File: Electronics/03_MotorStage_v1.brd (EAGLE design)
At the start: 100 x 80 mm, 77 parts, among them J1 BARRIER_BLOCK-2PIN, J2 BARRIER_BLOCK-5PIN, J3 CONN_2X3_SMD, U1 XL4016-DEV

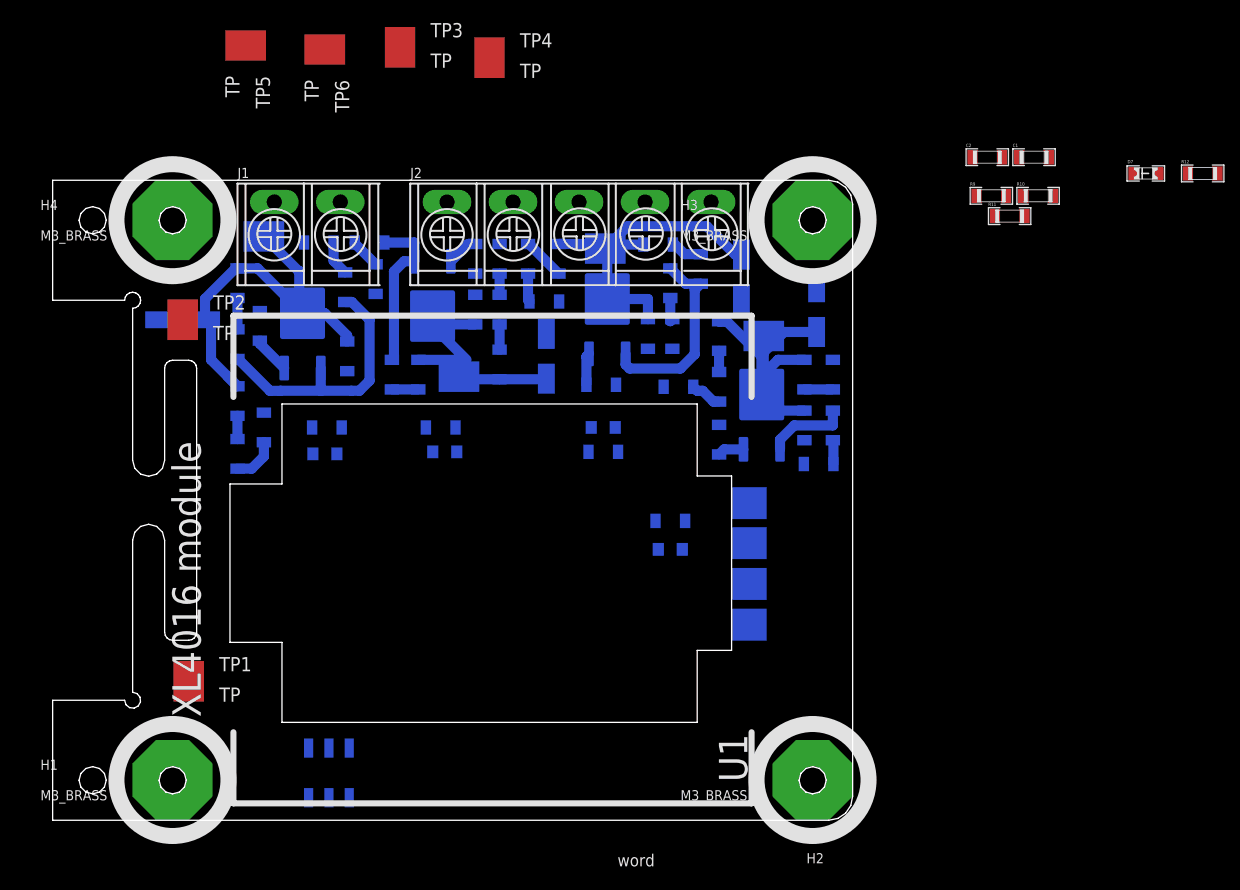
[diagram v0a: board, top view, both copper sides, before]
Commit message: Completed routing of components on motor stage power supply board
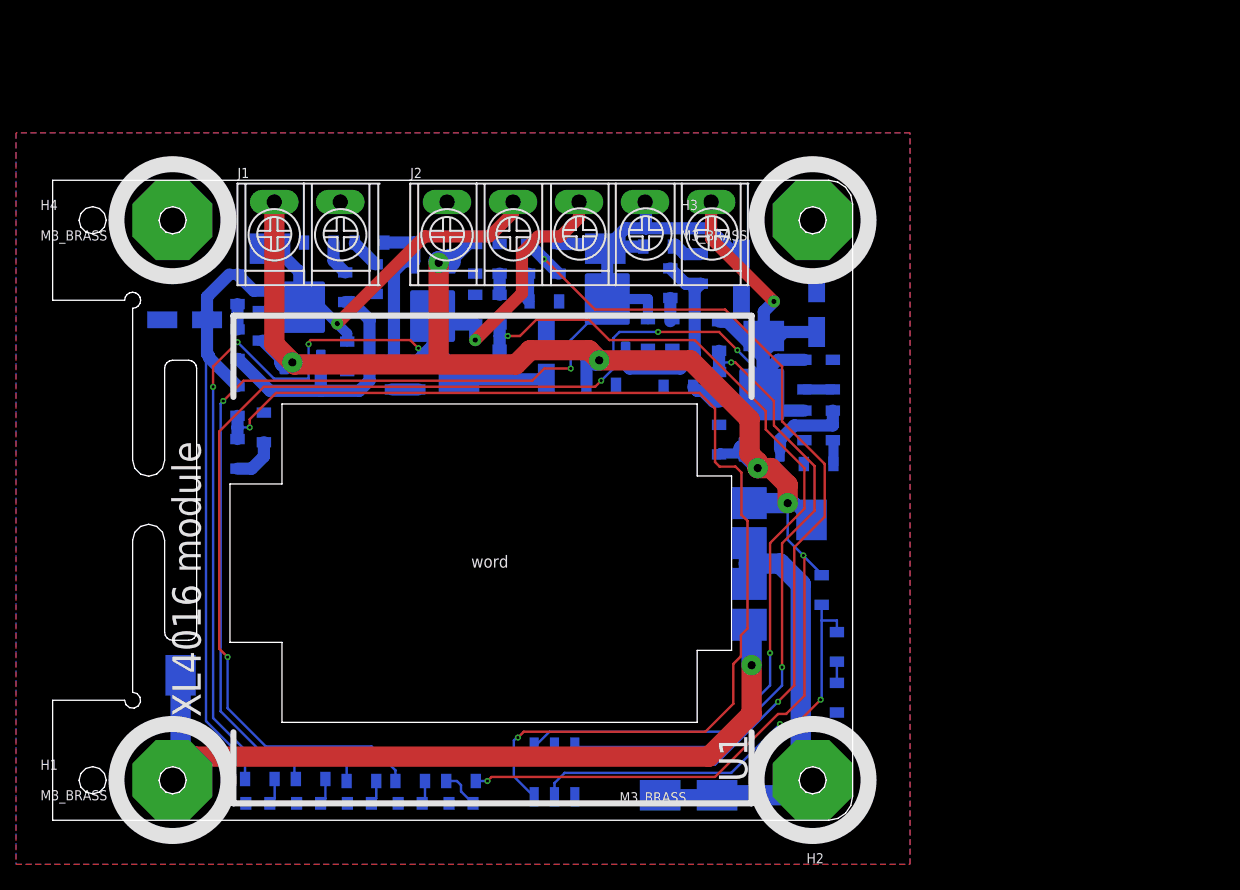
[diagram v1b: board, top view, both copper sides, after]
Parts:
- removed C1: 0.33 uF, standardparts:1206
- removed C2: 10 uF, standardparts:1206
- removed TP5, TP6: TP, Hippo-PS:TP
- C10, C4, C6, C8: value (none) -> 22 uF
- C3, C5, C7, C9: value (none) -> 10 uF
- D7: value YELLOW -> ORANGE
- R10: value 2K -> 4.7K
- R11: value 220 -> 330
- R12: value 220 -> 470
- moved R12 119.8 mm to (68.3, 23.1), flipped to the bottom
- moved D7 116.3 mm to (68.3, 20.3), flipped to the bottom
- moved TP4 94.6 mm to (93.2, 21.3), flipped to the bottom, turned to 270 degrees
- moved TP2 89.4 mm to (100.3, 21.3), flipped to the bottom, turned to 90 degrees
- moved TP3 78.3 mm to (112.1, 55.8), flipped to the bottom
- moved R11 64.0 mm to (115.3, 33.5), flipped to the bottom, turned to 270 degrees
- moved R10 61.7 mm to (115.3, 39.9), flipped to the bottom, turned to 270 degrees
- moved D3 56.0 mm to (55.6, 20.3)
- moved R9 53.6 mm to (113.4, 47.0), flipped to the bottom, turned to 270 degrees
- moved R31 51.1 mm to (55.9, 23.1), turned to 180 degrees
- moved D2 47.1 mm to (49.3, 20.3)
- moved R22 46.9 mm to (49.5, 23.4), turned to 180 degrees
- moved R40 46.0 mm to (62.0, 23.1), turned to 180 degrees
- moved D4 45.4 mm to (62.0, 20.3)
- moved R13 44.7 mm to (43.2, 23.4)
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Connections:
- removed net N$2: U1.IN-, U1.OUT-
- new net IN+: H1.P$1, H3.P$1, TP1.P$1, U1.IN+
- new net N$1: D7.P$1, R12.2
- new net N$23: R10.2, R11.1
- new net SIG_SMPS: J3.4, R10.1, R9.2
- net GND: now also D7.P$2, H2.P$1, H4.P$1, J2.P$1, J3.6, R11.2, TP2.P$1, TP4.P$1, U1.IN-, U1.OUT-
- net OUT1: now also J2.P$2
- net OUT2: now also J2.P$3
- net OUT3: now also J2.P$4
- net OUT4: now also J2.P$5
- net SIG1: now also J3.2
- net SIG2: now also J3.1
- net SIG3: now also J3.3
- net SIG4: now also J3.5
- net V+: now also R12.1, R9.1, TP3.P$1, U1.OUT+
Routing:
- net V+: track 15.9 -> 213.8 mm, vias 0 -> 7
- net OUT4: track 47.0 -> 208.0 mm, vias 0 -> 5
- net SIG1: track 2.90 -> 143.7 mm, vias 0 -> 2
- net OUT3: track 44.7 -> 163.2 mm, vias 0 -> 2
- net OUT2: track 31.4 -> 148.8 mm, vias 0 -> 5
- net SIG3: track 5.34 -> 120.2 mm, vias 0 -> 2
- net SIG2: track 3.16 -> 112.7 mm, vias 0 -> 2
- net IN+: track 0.00 -> 100.6 mm, vias 0 -> 1
- net OUT1: track 50.1 -> 130.7 mm, vias 0 -> 1
- net SIG4: track 2.65 -> 79.9 mm, vias 0 -> 2
- net GND: track 0.00 -> 57.7 mm
- net SIG_SMPS: track 0.00 -> 54.6 mm, vias 0 -> 2
- net N$1: track 0.00 -> 4.97 mm
- net N$3: track 0.00 -> 3.30 mm
- net N$10: track 0.00 -> 3.30 mm
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- added copper zone on layer 1, net GND
- added copper zone on layer 16, net GND
